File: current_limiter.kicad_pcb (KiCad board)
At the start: 4 copper layers, 64.5 x 28 mm, 47 parts, among them J1 VIN, J2 VOUT, J3 CS-, J4 CS+, Q1 BSC040N10NS5, Q2 BC849, Q3 BC858, U1 TLV1805QDBVRQ1, U2 INA181A2IDBVR, U3 OPA991IDCKR, U4 BAT54CLT3G, U5 LM4040DIM3-2.5/NOPB

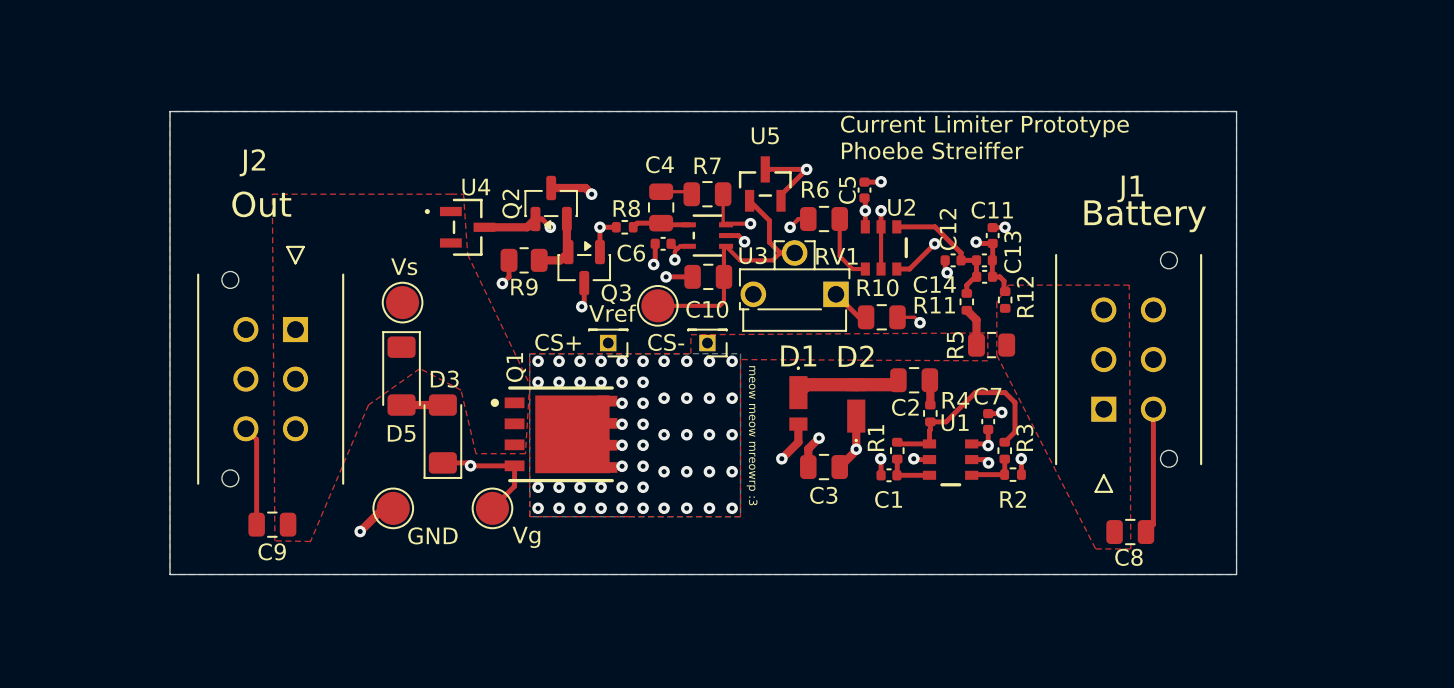
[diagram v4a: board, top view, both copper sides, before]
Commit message: minor revisions, changed molex to banana plug and readjusted zones
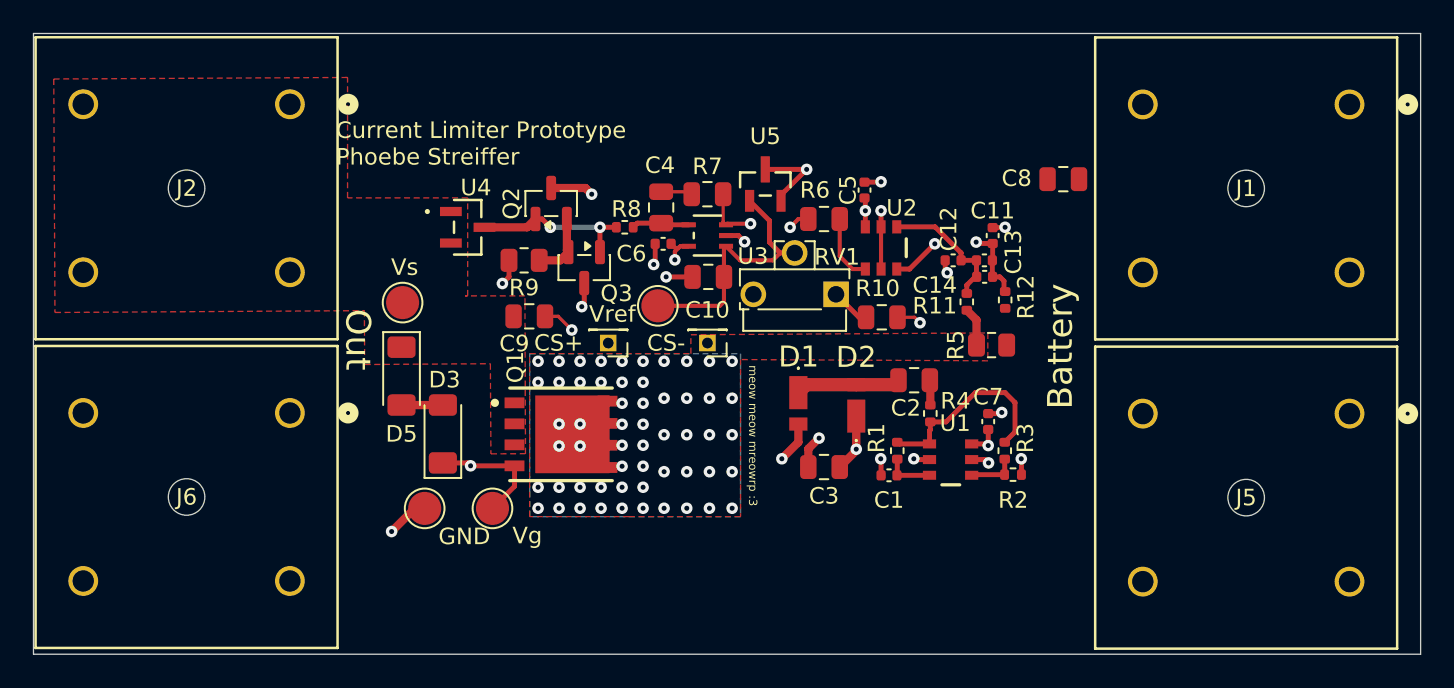
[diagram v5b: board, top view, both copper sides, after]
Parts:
- added J5: 73096-2, Current_Limiter_Stuff:CONN_73096-2_POM, F.Cu at (170.8, 48.3)
- added J6: 73096-2, Current_Limiter_Stuff:CONN_73096-2_POM, F.Cu at (106.8, 48.2)
- J1: value VIN -> 73096-2; footprint Current_Limiter_Stuff:4304506YY_6 -> Current_Limiter_Stuff:CONN_73096-2_POM
- J2: value VOUT -> 73096-2; footprint Current_Limiter_Stuff:4304506YY_6 -> Current_Limiter_Stuff:CONN_73096-2_POM
- moved J1 23.7 mm to (170.8, 29.6), turned to 0 degrees
- moved C8 21.7 mm to (153.5, 34.1), turned to 180 degrees
- moved C9 20.0 mm to (121.2, 42.4), turned to 0 degrees
- moved J2 13.6 mm to (106.8, 29.6), turned to 0 degrees
- moved TP4 1.90 mm to (114.9, 54.0)
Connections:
- J1 pad 4: GND -> +15V
- J2 pad 4: GND -> /VBATT
- U5 pad 3: GND -> unconnected-(U5-Pad3)
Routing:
- net VCC: track 30.8 -> 58.3 mm
- net GND: track 40.2 -> 27.7 mm, vias 16 -> 17
- net /CSA_IN-: vias 52 -> 56
- added copper zone on In2.Cu, net +15V
- added copper zone on In1.Cu, net GND
- removed copper zone on F.Cu, net +15V
- removed copper zone on In1.Cu, net +15V
- removed copper zone on B.Cu, net GND
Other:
- board size 64.5 x 28 mm -> 83.9 x 37.5 mm
